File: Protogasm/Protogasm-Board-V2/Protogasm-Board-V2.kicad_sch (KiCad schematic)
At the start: 10 parts, among them J1 Neopixel_Ring_Header, M1 Motor_DC, Q1 FQP30N06L, SW1 Rotary_Encoder_Switch, U1 Arduino_UNO_R3, U2 MPX5050GP

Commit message: Assign a few footprints (although we need to make some custom ones
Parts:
- C1: footprint (none) -> Capacitor_THT:C_Disc_D5.0mm_W2.5mm_P2.50mm
- D1: footprint (none) -> Diode_THT:D_A-405_P7.62mm_Horizontal
- J1: footprint (none) -> Connector:FanPinHeader_1x03_P2.54mm_Vertical
- M1: footprint (none) -> Connector_Molex:Molex_KK-396_A-41791-0002_1x02_P3.96mm_Vertical
- Q1: footprint (none) -> Package_TO_SOT_THT:TO-220-3_Horizontal_TabDown
- R1: footprint (none) -> Resistor_THT:R_Axial_DIN0207_L6.3mm_D2.5mm_P7.62mm_Horizontal
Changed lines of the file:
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@@
     (property "Reference" "J1" (id 0) (at 110.1598 79.629 0))
     (property "Value" "Neopixel_Ring_Header" (id 1) (at 110.1598 81.9404 0))
-    (property "Footprint" "" (id 2) (at 115.57 82.55 0)
+    (property "Footprint" "Connector:FanPinHeader_1x03_P2.54mm_Vertical" (id 2) (at 115.57 82.55 0)
       (effects (font (size 1.27 1.27)) hide)
     )
@@
       (effects (font (size 1.27 1.27)) (justify left))
     )
-    (property "Footprint" "" (id 2) (at 73.66 59.436 0)
+    (property "Footprint" "Connector_Molex:Molex_KK-396_A-41791-0002_1x02_P3.96mm_Vertical" (id 2) (at 73.66 59.436 0)
       (effects (font (size 1.27 1.27)) hide)
     )
@@
       (effects (font (size 1.27 1.27)) (justify right))
     )
-    (property "Footprint" "" (id 2) (at 66.04 58.42 0)
+    (property "Footprint" "Diode_THT:D_A-405_P7.62mm_Horizontal" (id 2) (at 66.04 58.42 0)
       (effects (font (size 1.27 1.27)) hide)
     )
@@
       (effects (font (size 1.27 1.27)) (justify left))
     )
-    (property "Footprint" "" (id 2) (at 71.12 73.66 0)
+    (property "Footprint" "Package_TO_SOT_THT:TO-220-3_Horizontal_TabDown" (id 2) (at 71.12 73.66 0)
       (effects (font (size 1.27 1.27)) hide)
     )
@@
       (effects (font (size 1.27 1.27)) (justify left))
     )
-    (property "Footprint" "" (id 2) (at 89.916 80.264 90)
+    (property "Footprint" "Resistor_THT:R_Axial_DIN0207_L6.3mm_D2.5mm_P7.62mm_Horizontal" (id 2) (at 89.916 80.264 90)
       (effects (font (size 1.27 1.27)) hide)
     )
@@
       (effects (font (size 1.27 1.27)) (justify left))
     )
-    (property "Footprint" "" (id 2) (at 216.8652 76.2 0)
+    (property "Footprint" "Capacitor_THT:C_Disc_D5.0mm_W2.5mm_P2.50mm" (id 2) (at 216.8652 76.2 0)
       (effects (font (size 1.27 1.27)) hide)
     )
@@
     )
     (path "/00000000-0000-0000-0000-000061e3d703"
-      (reference "C1") (unit 1) (value "0u1") (footprint "")
+      (reference "C1") (unit 1) (value "0u1") (footprint "Capacitor_THT:C_Disc_D5.0mm_W2.5mm_P2.50mm")
     )
     (path "/00000000-0000-0000-0000-000061e36e09"
-      (reference "D1") (unit 1) (value "1N5818-B") (footprint "")
+      (reference "D1") (unit 1) (value "1N5818-B") (footprint "Diode_THT:D_A-405_P7.62mm_Horizontal")
     )
     (path "/00000000-0000-0000-0000-000061e34a60"
-      (reference "J1") (unit 1) (value "Neopixel_Ring_Header") (footprint "")
+      (reference "J1") (unit 1) (value "Neopixel_Ring_Header") (footprint "Connector:FanPinHeader_1x03_P2.54mm_Vertical")
     )
     (path "/00000000-0000-0000-0000-000061e35097"
-      (reference "M1") (unit 1) (value "Motor_DC") (footprint "")
+      (reference "M1") (unit 1) (value "Motor_DC") (footprint "Connector_Molex:Molex_KK-396_A-41791-0002_1x02_P3.96mm_Vertical")
     )
     (path "/00000000-0000-0000-0000-000061e3bd27"
-      (reference "Q1") (unit 1) (value "FQP30N06L") (footprint "")
+      (reference "Q1") (unit 1) (value "FQP30N06L") (footprint "Package_TO_SOT_THT:TO-220-3_Horizontal_TabDown")
     )
     (path "/00000000-0000-0000-0000-000061e3c963"
-      (reference "R1") (unit 1) (value "220k") (footprint "")
+      (reference "R1") (unit 1) (value "220k") (footprint "Resistor_THT:R_Axial_DIN0207_L6.3mm_D2.5mm_P7.62mm_Horizontal")
     )
     (path "/00000000-0000-0000-0000-000061e35593"

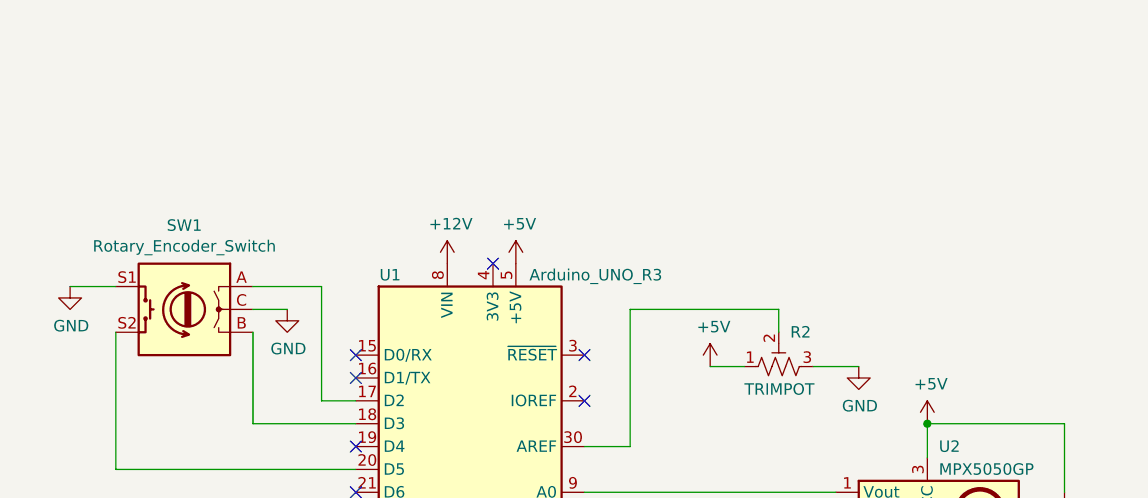
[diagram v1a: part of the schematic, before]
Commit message: Set up custom footprints
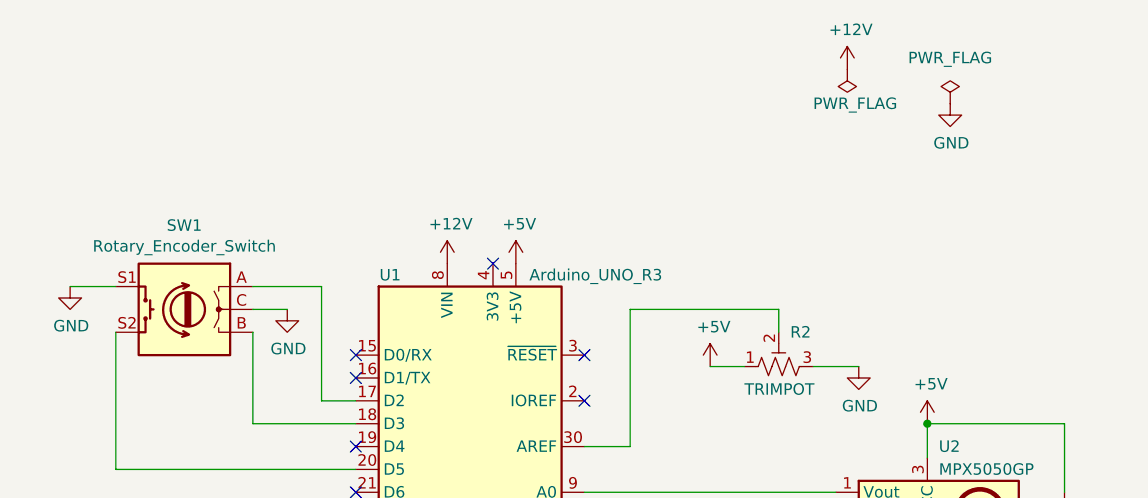
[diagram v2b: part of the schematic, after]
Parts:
- R2: footprint (none) -> custom-footprints:uxcell_TRIMPOT
- SW1: footprint (none) -> Rotary_Encoder:RotaryEncoder_Alps_EC12E-Switch_Vertical_H20mm
- U2: footprint (none) -> Connector_PinHeader_2.54mm:PinHeader_1x06_P2.54mm_Vertical
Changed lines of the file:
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@@
       (effects (font (size 1.27 1.27)) (justify right))
     )
-    (property "Footprint" "" (id 2) (at 184.15 54.61 0)
+    (property "Footprint" "custom-footprints:uxcell_TRIMPOT" (id 2) (at 184.15 54.61 0)
       (effects (font (size 1.27 1.27)) hide)
     )
@@
     (property "Reference" "SW1" (id 0) (at 118.11 38.9382 0))
     (property "Value" "Rotary_Encoder_Switch" (id 1) (at 118.11 41.2496 0))
-    (property "Footprint" "" (id 2) (at 121.92 44.196 0)
+    (property "Footprint" "Rotary_Encoder:RotaryEncoder_Alps_EC12E-Switch_Vertical_H20mm" (id 2) (at 121.92 44.196 0)
       (effects (font (size 1.27 1.27)) hide)
     )
@@
       (effects (font (size 1.27 1.27)) (justify right))
     )
-    (property "Footprint" "" (id 2) (at 213.36 81.28 0)
+    (property "Footprint" "Connector_PinHeader_2.54mm:PinHeader_1x06_P2.54mm_Vertical" (id 2) (at 213.36 81.28 0)
       (effects (font (size 1.27 1.27)) hide)
     )
@@
     (pin "1")
   )
+  (symbol (lib_id "power:+12V") (at 191.77 21.59 0) (unit 1)
+    (in_bom yes) (on_board yes)
+    (property "Reference" "#PWR01" (id 0) (at 191.77 25.4 0)
+      (effects (font (size 1.27 1.27)) hide)
+    )
+    (property "Value" "+12V" (id 1) (at 192.151 17.1958 0))
+    (property "Footprint" "" (id 2) (at 191.77 21.59 0)
+      (effects (font (size 1.27 1.27)) hide)
+    )
+    (property "Datasheet" "" (id 3) (at 191.77 21.59 0)
+      (effects (font (size 1.27 1.27)) hide)
+    )
+    (pin "1")
+  )
+  (symbol (lib_id "power:PWR_FLAG") (at 191.77 21.59 180) (unit 1)
+    (in_bom yes) (on_board yes)
+    (property "Reference" "#FLG01" (id 0) (at 191.77 23.495 0)
+      (effects (font (size 1.27 1.27)) hide)
+    )
+    (property "Value" "PWR_FLAG" (id 1) (at 187.96 25.4 0)
+      (effects (font (size 1.27 1.27)) (justify right))
+    )
+    (property "Footprint" "" (id 2) (at 191.77 21.59 0)
+      (effects (font (size 1.27 1.27)) hide)
+    )
+    (property "Datasheet" "~" (id 3) (at 191.77 21.59 0)
+      (effects (font (size 1.27 1.27)) hide)
+    )
+    (pin "1")
+  )
+  (symbol (lib_id "power:GND") (at 203.2 25.4 0) (unit 1)
+    (in_bom yes) (on_board yes)
+    (property "Reference" "#PWR02" (id 0) (at 203.2 31.75 0)
+      (effects (font (size 1.27 1.27)) hide)
+    )
+    (property "Value" "GND" (id 1) (at 203.327 29.7942 0))
+    (property "Footprint" "" (id 2) (at 203.2 25.4 0)
+      (effects (font (size 1.27 1.27)) hide)
+    )
+    (property "Datasheet" "" (id 3) (at 203.2 25.4 0)
+      (effects (font (size 1.27 1.27)) hide)
+    )
+    (pin "1")
+  )
+  (symbol (lib_id "power:PWR_FLAG") (at 203.2 25.4 0) (unit 1)
+    (in_bom yes) (on_board yes) (fields_autoplaced)
+    (property "Reference" "#FLG02" (id 0) (at 203.2 23.495 0)
+      (effects (font (size 1.27 1.27)) hide)
+    )
+    (property "Value" "PWR_FLAG" (id 1) (at 203.2 20.32 0))
+    (property "Footprint" "" (id 2) (at 203.2 25.4 0)
+      (effects (font (size 1.27 1.27)) hide)
+    )
+    (property "Datasheet" "~" (id 3) (at 203.2 25.4 0)
+      (effects (font (size 1.27 1.27)) hide)
+    )
+    (pin "1")
+  )
   (sheet_instances
     (path "/" (page "1"))
   )
   (symbol_instances
+    (path "/68f3fd88-6778-4ccc-879b-c4a57737e292"
+      (reference "#FLG01") (unit 1) (value "PWR_FLAG") (footprint "")
+    )
+    (path "/c526b1c7-4901-4110-8dfe-530311196312"
+      (reference "#FLG02") (unit 1) (value "PWR_FLAG") (footprint "")
+    )
+    (path "/265921f6-85e7-48ea-8cb2-b965324b3aec"
+      (reference "#PWR01") (unit 1) (value "+12V") (footprint "")
+    )
+    (path "/9593b9f1-af46-4166-97a6-596f109232fa"
+      (reference "#PWR02") (unit 1) (value "GND") (footprint "")
+    )
     (path "/00000000-0000-0000-0000-000061e4950b"
       (reference "#PWR0101") (unit 1) (value "+5V") (footprint "")
@@
     )
     (path "/00000000-0000-0000-0000-000061e35593"
-      (reference "R2") (unit 1) (value "TRIMPOT") (footprint "")
+      (reference "R2") (unit 1) (value "TRIMPOT") (footprint "custom-footprints:uxcell_TRIMPOT")
     )
     (path "/00000000-0000-0000-0000-000061e362a6"
-      (reference "SW1") (unit 1) (value "Rotary_Encoder_Switch") (footprint "")
+      (reference "SW1") (unit 1) (value "Rotary_Encoder_Switch") (footprint "Rotary_Encoder:RotaryEncoder_Alps_EC12E-Switch_Vertical_H20mm")
     )
     (path "/00000000-0000-0000-0000-000061e31d9c"
@@
     )
     (path "/00000000-0000-0000-0000-000061e369b7"
-      (reference "U2") (unit 1) (value "MPX5050GP") (footprint "")
-    )
-  )
+      (reference "U2") (unit 1) (value "MPX5050GP") (footprint "Connector_PinHeader_2.54mm:PinHeader_1x06_P2.54mm_Vertical")
+    )
+  )

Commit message: Finished the custom footprints
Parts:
- J1: footprint Connector:FanPinHeader_1x03_P2.54mm_Vertical -> custom-footprints:Neopixel_Ring_WirePins
- M1: footprint Connector_Molex:Molex_KK-396_A-41791-0002_1x02_P3.96mm_Vertical -> custom-footprints:Motor_DC_WirePins
- U1: footprint Module:Arduino_UNO_R3 -> Module:Arduino_UNO_R3_WithMountingHoles
- U2: footprint Connector_PinHeader_2.54mm:PinHeader_1x06_P2.54mm_Vertical -> custom-footprints:MPX5050GP
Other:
- moved on the sheet: C1, D1, J1, M1, Q1, R1, R2, SW1, U1, U2

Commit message: Finalize protogasm board V2 (the basic remake)
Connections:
- net D2: now reaches SW1.A, U1.17 (D2)
- net D3: now reaches SW1.B, U1.18 (D3)
- net D5: now reaches SW1.S2, U1.20 (D5)
- net D9: now reaches Q1.1 (G), R1.1, U1.24 (D9)
- net D10: now reaches J1.2 (Data_Input), U1.25 (D10)
- net AREF: now reaches R2.2, U1.30 (AREF)
- net A0: now reaches U1.9 (A0), U2.1 (Vout)
- net MOTOR-: now reaches D1.2 (A), M1.2 (-), Q1.2 (D)
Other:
- moved on the sheet: D1, SW1
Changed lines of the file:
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@@
   (no_connect (at 134.62 87.63))
   (no_connect (at 134.62 97.79))
-  (wire (pts (xy 123.19 95.25) (xy 123.19 85.09))
+  (wire (pts (xy 119.38 95.25) (xy 119.38 85.09))
     (stroke (width 0) (type default) (color 0 0 0 0))
   )
@@
     (stroke (width 0) (type default) (color 0 0 0 0))
   )
-  (wire (pts (xy 181.61 82.55) (xy 165.1 82.55))
-    (stroke (width 0) (type default) (color 0 0 0 0))
-  )
-  (wire (pts (xy 134.62 92.71) (xy 130.81 92.71))
-    (stroke (width 0) (type default) (color 0 0 0 0))
-  )
-  (wire (pts (xy 102.87 80.01) (xy 107.95 80.01))
+  (wire (pts (xy 181.61 82.55) (xy 167.64 82.55))
+    (stroke (width 0) (type default) (color 0 0 0 0))
+  )
+  (wire (pts (xy 134.62 92.71) (xy 128.27 92.71))
+    (stroke (width 0) (type default) (color 0 0 0 0))
+  )
+  (wire (pts (xy 99.06 80.01) (xy 104.14 80.01))
     (stroke (width 0) (type default) (color 0 0 0 0))
   )
@@
     (stroke (width 0) (type default) (color 0 0 0 0))
   )
-  (wire (pts (xy 63.5 100.33) (xy 63.5 96.52))
+  (wire (pts (xy 60.96 100.33) (xy 60.96 96.52))
     (stroke (width 0) (type default) (color 0 0 0 0))
   )
@@
     (stroke (width 0) (type default) (color 0 0 0 0))
   )
-  (wire (pts (xy 71.12 83.82) (xy 63.5 83.82))
-    (stroke (width 0) (type default) (color 0 0 0 0))
-  )
-  (wire (pts (xy 130.81 80.01) (xy 123.19 80.01))
+  (wire (pts (xy 71.12 83.82) (xy 60.96 83.82))
+    (stroke (width 0) (type default) (color 0 0 0 0))
+  )
+  (wire (pts (xy 128.27 80.01) (xy 119.38 80.01))
     (stroke (width 0) (type default) (color 0 0 0 0))
   )
@@
     (stroke (width 0) (type default) (color 0 0 0 0))
   )
-  (wire (pts (xy 107.95 100.33) (xy 134.62 100.33))
-    (stroke (width 0) (type default) (color 0 0 0 0))
-  )
-  (wire (pts (xy 160.02 97.79) (xy 165.1 97.79))
+  (wire (pts (xy 104.14 100.33) (xy 134.62 100.33))
+    (stroke (width 0) (type default) (color 0 0 0 0))
+  )
+  (wire (pts (xy 160.02 97.79) (xy 167.64 97.79))
     (stroke (width 0) (type default) (color 0 0 0 0))
   )
@@
     (stroke (width 0) (type default) (color 0 0 0 0))
   )
-  (wire (pts (xy 71.12 100.33) (xy 63.5 100.33))
-    (stroke (width 0) (type default) (color 0 0 0 0))
-  )
-  (wire (pts (xy 165.1 82.55) (xy 165.1 97.79))
-    (stroke (width 0) (type default) (color 0 0 0 0))
-  )
-  (wire (pts (xy 127 82.55) (xy 123.19 82.55))
+  (wire (pts (xy 71.12 100.33) (xy 60.96 100.33))
+    (stroke (width 0) (type default) (color 0 0 0 0))
+  )
+  (wire (pts (xy 167.64 82.55) (xy 167.64 97.79))
+    (stroke (width 0) (type default) (color 0 0 0 0))
+  )
+  (wire (pts (xy 119.38 82.55) (xy 123.19 82.55))
     (stroke (width 0) (type default) (color 0 0 0 0))
   )
@@
     (stroke (width 0) (type default) (color 0 0 0 0))
   )
-  (wire (pts (xy 107.95 100.33) (xy 107.95 85.09))
+  (wire (pts (xy 104.14 100.33) (xy 104.14 85.09))
     (stroke (width 0) (type default) (color 0 0 0 0))
   )
@@
     (stroke (width 0) (type default) (color 0 0 0 0))
   )
-  (wire (pts (xy 63.5 83.82) (xy 63.5 88.9))
+  (wire (pts (xy 60.96 83.82) (xy 60.96 88.9))
     (stroke (width 0) (type default) (color 0 0 0 0))
   )
@@
     (stroke (width 0) (type default) (color 0 0 0 0))
   )
-  (wire (pts (xy 134.62 95.25) (xy 123.19 95.25))
-    (stroke (width 0) (type default) (color 0 0 0 0))
-  )
-  (wire (pts (xy 130.81 92.71) (xy 130.81 80.01))
+  (wire (pts (xy 134.62 95.25) (xy 119.38 95.25))
+    (stroke (width 0) (type default) (color 0 0 0 0))
+  )
+  (wire (pts (xy 128.27 92.71) (xy 128.27 80.01))
     (stroke (width 0) (type default) (color 0 0 0 0))
   )
   (wire (pts (xy 198.12 99.06) (xy 198.12 95.25))
     (stroke (width 0) (type default) (color 0 0 0 0))
+  )
+  (label "D2" (at 128.27 92.71 0)
+    (effects (font (size 1.27 1.27)) (justify left bottom))
+  )
+  (label "D10" (at 128.27 113.03 0)
+    (effects (font (size 1.27 1.27)) (justify left bottom))
+  )
+  (label "AREF" (at 162.56 97.79 0)
+    (effects (font (size 1.27 1.27)) (justify left bottom))
+  )
+  (label "D5" (at 128.27 100.33 0)
+    (effects (font (size 1.27 1.27)) (justify left bottom))
+  )
+  (label "D9" (at 128.27 110.49 0)
+    (effects (font (size 1.27 1.27)) (justify left bottom))
+  )
+  (label "D3" (at 128.27 95.25 0)
+    (effects (font (size 1.27 1.27)) (justify left bottom))
+  )
+  (label "A0" (at 162.56 102.87 0)
+    (effects (font (size 1.27 1.27)) (justify left bottom))
+  )
+  (label "MOTOR-" (at 60.96 100.33 0)
+    (effects (font (size 1.27 1.27)) (justify left bottom))
   )
   (symbol (lib_id "MCU_Module:Arduino_UNO_R3") (at 147.32 102.87 0) (unit 1)
@@
     (pin "3")
   )
-  (symbol (lib_id "Device:Rotary_Encoder_Switch") (at 115.57 82.55 0) (mirror y) (unit 1)
-    (in_bom yes) (on_board yes)
-    (property "Reference" "SW1" (id 0) (at 115.57 73.2282 0))
-    (property "Value" "Rotary_Encoder_Switch" (id 1) (at 115.57 75.5396 0))
-    (property "Footprint" "Rotary_Encoder:RotaryEncoder_Alps_EC12E-Switch_Vertical_H20mm" (id 2) (at 119.38 78.486 0)
-      (effects (font (size 1.27 1.27)) hide)
-    )
-    (property "Datasheet" "~" (id 3) (at 115.57 75.946 0)
+  (symbol (lib_id "Device:Rotary_Encoder_Switch") (at 111.76 82.55 0) (mirror y) (unit 1)
+    (in_bom yes) (on_board yes)
+    (property "Reference" "SW1" (id 0) (at 111.76 73.2282 0))
+    (property "Value" "Rotary_Encoder_Switch" (id 1) (at 111.76 75.5396 0))
+    (property "Footprint" "Rotary_Encoder:RotaryEncoder_Alps_EC12E-Switch_Vertical_H20mm" (id 2) (at 115.57 78.486 0)
+      (effects (font (size 1.27 1.27)) hide)
+    )
+    (property "Datasheet" "~" (id 3) (at 111.76 75.946 0)
       (effects (font (size 1.27 1.27)) hide)
     )
@@
     (pin "6")
   )
-  (symbol (lib_id "Device:D") (at 63.5 92.71 270) (unit 1)
-    (in_bom yes) (on_board yes)
-    (property "Reference" "D1" (id 0) (at 60.96 91.44 90)
-      (effects (font (size 1.27 1.27)) (justify right))
-    )
-    (property "Value" "1N5818-B" (id 1) (at 60.96 93.98 90)
-      (effects (font (size 1.27 1.27)) (justify right))
-    )
-    (property "Footprint" "Diode_THT:D_A-405_P7.62mm_Horizontal" (id 2) (at 63.5 92.71 0)
-      (effects (font (size 1.27 1.27)) hide)
-    )
-    (property "Datasheet" "~" (id 3) (at 63.5 92.71 0)
+  (symbol (lib_id "Device:D") (at 60.96 92.71 270) (unit 1)
+    (in_bom yes) (on_board yes)
+    (property "Reference" "D1" (id 0) (at 58.42 91.44 90)
+      (effects (font (size 1.27 1.27)) (justify right))
+    )
+    (property "Value" "1N5818-B" (id 1) (at 58.42 93.98 90)
+      (effects (font (size 1.27 1.27)) (justify right))
+    )
+    (property "Footprint" "Diode_THT:D_A-405_P7.62mm_Horizontal" (id 2) (at 60.96 92.71 0)
+      (effects (font (size 1.27 1.27)) hide)
+    )
+    (property "Datasheet" "~" (id 3) (at 60.96 92.71 0)
       (effects (font (size 1.27 1.27)) hide)
     )
@@
     (pin "1")
   )
-  (symbol (lib_id "power:GND") (at 127 82.55 0) (unit 1)
-    (in_bom yes) (on_board yes)
-    (property "Reference" "#PWR0105" (id 0) (at 127 88.9 0)
-      (effects (font (size 1.27 1.27)) hide)
-    )
-    (property "Value" "GND" (id 1) (at 127.127 86.9442 0))
-    (property "Footprint" "" (id 2) (at 127 82.55 0)
-      (effects (font (size 1.27 1.27)) hide)
-    )
-    (property "Datasheet" "" (id 3) (at 127 82.55 0)
-      (effects (font (size 1.27 1.27)) hide)
-    )
-    (pin "1")
-  )
-  (symbol (lib_id "power:GND") (at 102.87 80.01 0) (unit 1)
-    (in_bom yes) (on_board yes)
-    (property "Reference" "#PWR0106" (id 0) (at 102.87 86.36 0)
-      (effects (font (size 1.27 1.27)) hide)
-    )
-    (property "Value" "GND" (id 1) (at 102.997 84.4042 0))
-    (property "Footprint" "" (id 2) (at 102.87 80.01 0)
-      (effects (font (size 1.27 1.27)) hide)
-    )
-    (property "Datasheet" "" (id 3) (at 102.87 80.01 0)
-      (effects (font (size 1.27 1.27)) hide)
-    )
+  (symbol (lib_id "power:GND") (at 123.19 82.55 0) (unit 1)
+    (in_bom yes) (on_board yes)
+    (property "Reference" "#PWR0105" (id 0) (at 123.19 88.9 0)
+      (effects (font (size 1.27 1.27)) hide)
+    )
+    (property "Value" "GND" (id 1) (at 123.317 86.9442 0))
+    (property "Footprint" "" (id 2) (at 123.19 82.55 0)
+      (effects (font (size 1.27 1.27)) hide)
+    )
+    (property "Datasheet" "" (id 3) (at 123.19 82.55 0)
+      (effects (font (size 1.27 1.27)) hide)
+    )
+    (pin "1")
+  )
+  (symbol (lib_id "power:GND") (at 99.06 80.01 0) (unit 1)
+    (in_bom yes) (on_board yes)
+    (property "Reference" "#PWR0106" (id 0) (at 99.06 86.36 0)
+      (effects (font (size 1.27 1.27)) hide)
+    )
+    (property "Value" "GND" (id 1) (at 99.187 84.4042 0))
+    (property "Footprint" "" (id 2) (at 99.06 80.01 0)
+      (effects (font (size 1.27 1.27)) hide)
+    )
+    (property "Datasheet" "" (id 3) (at 99.06 80.01 0)
+      (effects (font (size 1.27 1.27)) hide)
+    )
